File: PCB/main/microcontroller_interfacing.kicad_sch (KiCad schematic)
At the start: 16 parts, among them IC5 CP2102-GMR, U3 CAT24C256, U4 MICROXNJ

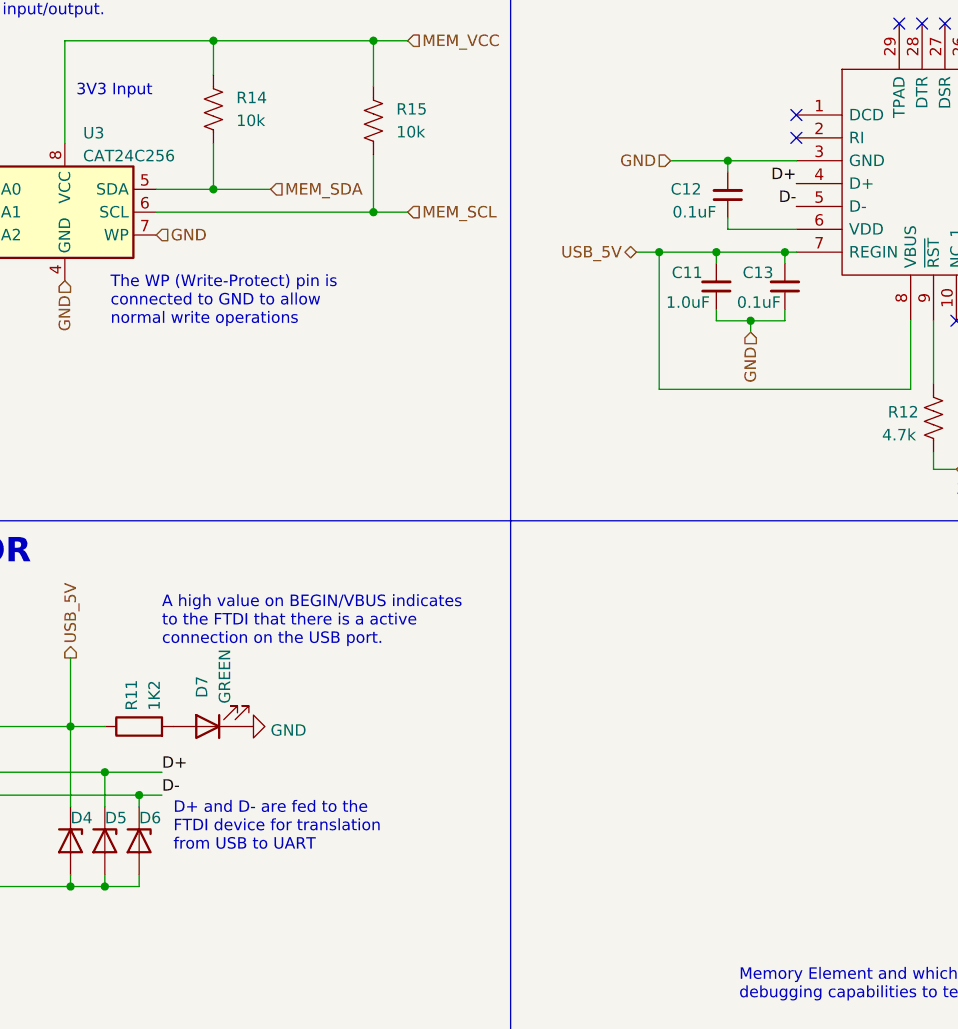
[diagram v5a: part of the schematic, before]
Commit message: Updated PCB with testpads
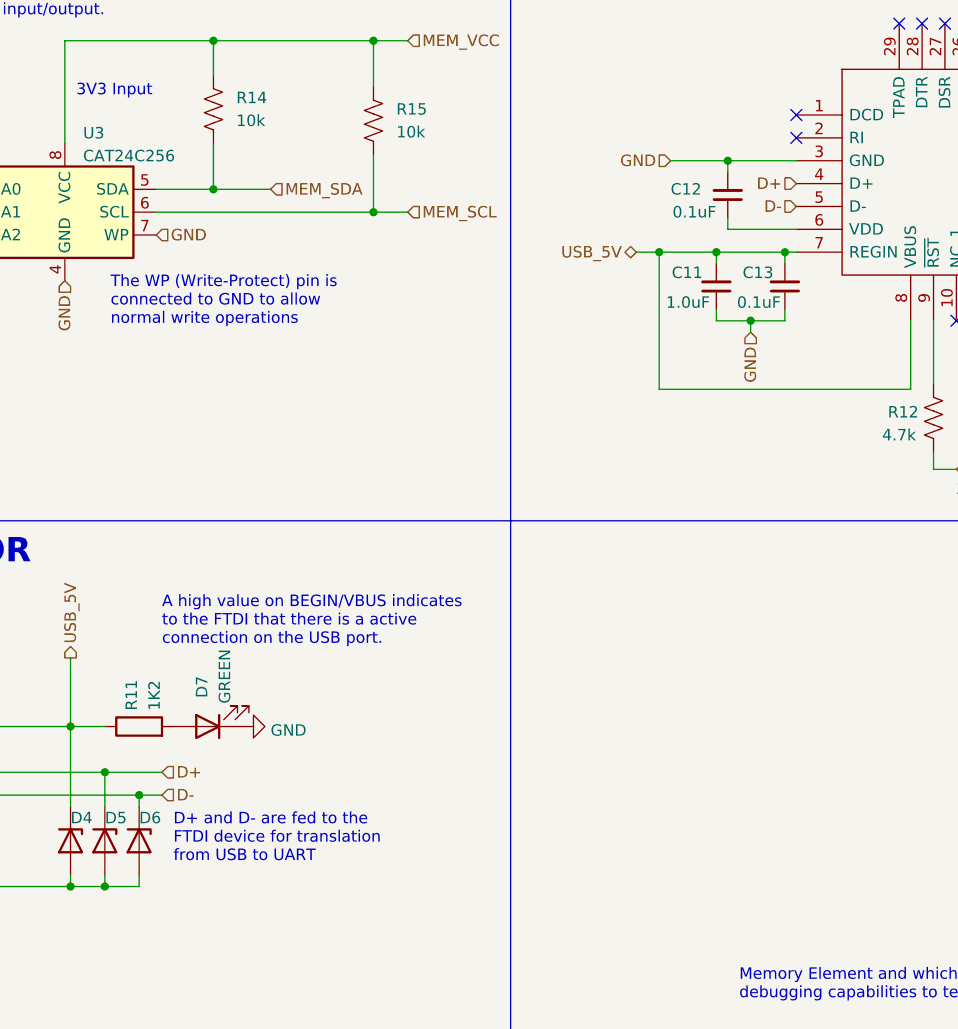
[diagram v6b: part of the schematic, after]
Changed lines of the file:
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@@
   )
   (text "D+ and D- are fed to the\nFTDI device for translation \nfrom USB to UART"
-    (at 64.135 115.57 0)
+    (at 64.135 116.84 0)
     (effects (font (size 1.27 1.27)) (justify left bottom))
   )
@@
   )
   (text "3V3 Input\n" (at 151.13 76.2 0)
-    (effects (font (size 1.27 1.27)) (justify left bottom))
-  )
-  (label "D+" (at 133.35 41.275 180)
-    (effects (font (size 1.27 1.27)) (justify right bottom))
-  )
-  (label "D+" (at 62.865 106.68 0)
-    (effects (font (size 1.27 1.27)) (justify left bottom))
-  )
-  (label "D-" (at 133.35 43.815 180)
-    (effects (font (size 1.27 1.27)) (justify right bottom))
-  )
-  (label "D-" (at 62.865 109.22 0)
     (effects (font (size 1.27 1.27)) (justify left bottom))
   )
@@
     (effects (font (size 1.27 1.27)) (justify left))
   )
+  (hierarchical_label "D+" (shape input) (at 62.865 106.68 0)
+    (effects (font (size 1.27 1.27)) (justify left))
+  )
   (hierarchical_label "FTDI_VDD" (shape input) (at 151.13 73.025 0)
     (effects (font (size 1.27 1.27)) (justify left))
@@
   )
   (hierarchical_label "GND" (shape input) (at 128.27 57.785 270)
+    (effects (font (size 1.27 1.27)) (justify right))
+  )
+  (hierarchical_label "D+" (shape input) (at 133.35 41.275 180)
+    (effects (font (size 1.27 1.27)) (justify right))
+  )
+  (hierarchical_label "D-" (shape input) (at 133.35 43.815 180)
     (effects (font (size 1.27 1.27)) (justify right))
   )
@@
     (effects (font (size 1.27 1.27)) (justify left))
   )
+  (hierarchical_label "D-" (shape input) (at 62.865 109.22 0)
+    (effects (font (size 1.27 1.27)) (justify left))
+  )

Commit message: Finished Gerbers and updated BOM
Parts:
- C11: LCSC (none) -> C15849
- C12, C13: LCSC (none) -> C1525
- D4, D5, D6: LCSC (none) -> C8056
- D7, D8: LCSC (none) -> C72043
- IC5: LCSC (none) -> C6568
- R11, R13: LCSC (none) -> C22765
- R12: value 4.7k -> 4k7; footprint EEE3088F_Footprints:RESC2013X65N -> EEE3088F_Footprints:RESC1608X55N; LCSC (none) -> C23162
- R14, R15: LCSC (none) -> C25804
- U3: LCSC (none) -> C6482
- U4: LCSC (none) -> C404969
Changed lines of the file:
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@@
       (effects (font (size 1.27 1.27)) (justify left) hide)
+    )
+    (property "LCSC" "C6568" (id 12) (at 149.86 45.085 0)
+      (effects (font (size 1.27 1.27)) hide)
     )
     (pin "1")
@@
       (effects (font (size 1.27 1.27)) (justify right))
     )
-    (property "Value" "4.7k" (id 1) (at 142.875 69.215 0)
-      (effects (font (size 1.27 1.27)) (justify right))
-    )
-    (property "Footprint" "EEE3088F_Footprints:RESC2013X65N" (id 2) (at 147.574 67.056 90)
+    (property "Value" "4k7" (id 1) (at 142.875 69.215 0)
+      (effects (font (size 1.27 1.27)) (justify right))
+    )
+    (property "Footprint" "EEE3088F_Footprints:RESC1608X55N" (id 2) (at 147.574 67.056 90)
       (effects (font (size 1.27 1.27)) hide)
     )
@@
       (effects (font (size 1.27 1.27)) hide)
     )
+    (property "LCSC" "C23162" (id 4) (at 148.59 67.31 0)
+      (effects (font (size 1.27 1.27)) hide)
+    )
     (pin "1")
     (pin "2")
@@
     )
     (property "Datasheet" "https://www.onsemi.cn/PowerSolutions/document/CAT24C256-D.PDF" (id 3) (at 52.07 44.45 0)
+      (effects (font (size 1.27 1.27)) hide)
+    )
+    (property "LCSC" "C6482" (id 4) (at 52.07 44.45 0)
       (effects (font (size 1.27 1.27)) hide)
     )
@@
       (effects (font (size 1.27 1.27)) hide)
     )
+    (property "LCSC" "C1525" (id 4) (at 132.08 52.705 0)
+      (effects (font (size 1.27 1.27)) hide)
+    )
     (pin "1")
     (pin "2")
@@
       (effects (font (size 1.27 1.27)) hide)
     )
+    (property "LCSC" "C1525" (id 4) (at 125.73 42.545 0)
+      (effects (font (size 1.27 1.27)) hide)
+    )
     (pin "1")
     (pin "2")
@@
       (effects (font (size 1.27 1.27)) hide)
     )
+    (property "LCSC" "C72043" (id 4) (at 182.245 58.42 90)
+      (effects (font (size 1.27 1.27)) hide)
+    )
     (pin "1")
     (pin "2")
@@
       (effects (font (size 1.27 1.27)) hide)
     )
+    (property "LCSC" "C22765" (id 4) (at 60.325 101.6 0)
+      (effects (font (size 1.27 1.27)) hide)
+    )
     (pin "1")
     (pin "2")
@@
       (effects (font (size 1.27 1.27)) hide)
     )
+    (property "LCSC" "C72043" (id 4) (at 67.945 101.6 90)
+      (effects (font (size 1.27 1.27)) hide)
+    )
     (pin "1")
     (pin "2")
@@
       (effects (font (size 1.27 1.27)) hide)
     )
+    (property "LCSC" "C25804" (id 4) (at 68.58 33.02 0)
+      (effects (font (size 1.27 1.27)) hide)
+    )
     (pin "1")
     (pin "2")
@@
       (effects (font (size 1.27 1.27)) hide)
     )
+    (property "LCSC" "C15849" (id 4) (at 124.46 52.705 0)
+      (effects (font (size 1.27 1.27)) hide)
+    )
     (pin "1")
     (pin "2")
@@
     )
     (property "Datasheet" "~" (id 3) (at 86.36 34.29 0)
+      (effects (font (size 1.27 1.27)) hide)
+    )
+    (property "LCSC" "C25804" (id 4) (at 86.36 34.29 0)
       (effects (font (size 1.27 1.27)) hide)
     )
@@
       (effects (font (size 1.27 1.27)) hide)
     )
+    (property "LCSC" "C8056" (id 4) (at 52.705 114.3 90)
+      (effects (font (size 1.27 1.27)) hide)
+    )
     (pin "1")
     (pin "2")
@@
     )
     (property "Datasheet" "" (id 3) (at 33.655 106.68 0)
+      (effects (font (size 1.27 1.27)) hide)
+    )
+    (property "LCSC" "C404969" (id 4) (at 33.655 106.68 0)
       (effects (font (size 1.27 1.27)) hide)
     )
@@
       (effects (font (size 1.27 1.27)) hide)
     )
+    (property "LCSC" "C8056" (id 4) (at 60.325 114.3 90)
+      (effects (font (size 1.27 1.27)) hide)
+    )
     (pin "1")
     (pin "2")
@@
       (effects (font (size 1.27 1.27)) hide)
     )
+    (property "LCSC" "C8056" (id 4) (at 56.515 114.3 90)
+      (effects (font (size 1.27 1.27)) hide)
+    )
     (pin "1")
     (pin "2")
@@
       (effects (font (size 1.27 1.27)) hide)
     )
+    (property "LCSC" "C22765" (id 4) (at 174.625 58.42 0)
+      (effects (font (size 1.27 1.27)) hide)
+    )
